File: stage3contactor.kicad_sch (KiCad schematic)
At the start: 3 parts, among them J20 Screw_Terminal_01x06, J21 Screw_Terminal_01x06, J22 Screw_Terminal_01x06

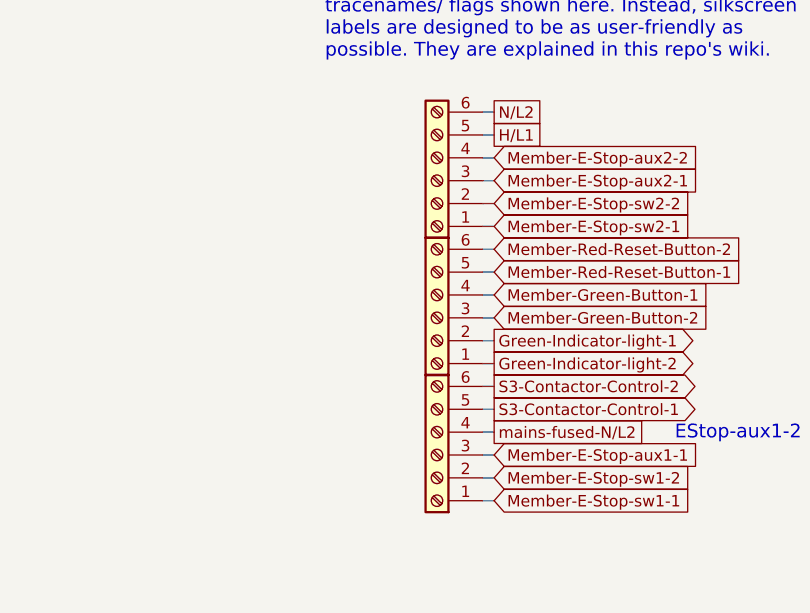
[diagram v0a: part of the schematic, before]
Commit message: 5v binary current and cleanup
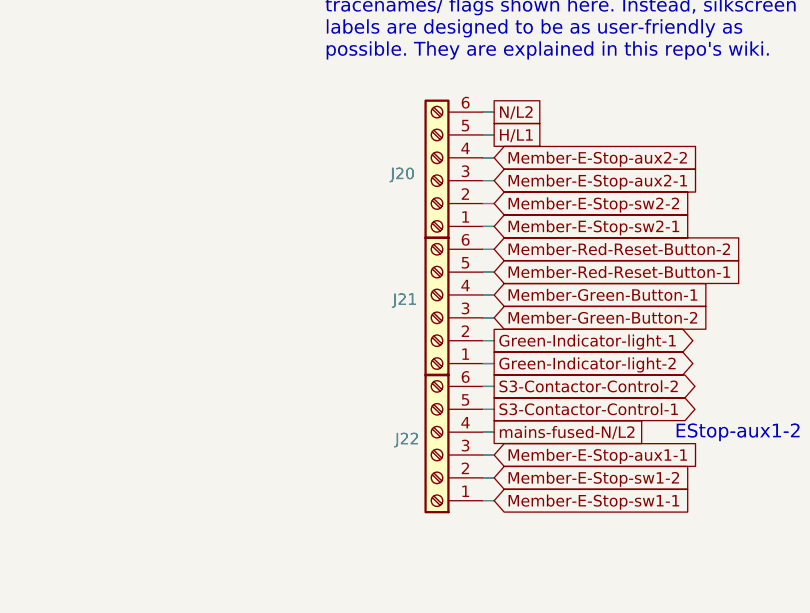
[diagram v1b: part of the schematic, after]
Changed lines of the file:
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@@
 		(on_board yes)
 		(dnp no)
-		(fields_autoplaced yes)
 		(property "Reference" "J20"
-			(at 184.15 78.74 0)
+			(at 180.34 91.948 0)
 			(effects
 				(font
 					(size 1.27 1.27)
 				)
-				(hide yes)
 			)
 		)
@@
 		(on_board yes)
 		(dnp no)
-		(fields_autoplaced yes)
 		(property "Reference" "J21"
-			(at 184.15 93.98 0)
+			(at 180.594 105.918 0)
 			(effects
 				(font
 					(size 1.27 1.27)
 				)
-				(hide yes)
 			)
 		)
@@
 		(on_board yes)
 		(dnp no)
-		(fields_autoplaced yes)
 		(property "Reference" "J22"
-			(at 184.15 109.22 0)
+			(at 180.848 121.412 0)
 			(effects
 				(font
 					(size 1.27 1.27)
 				)
-				(hide yes)
 			)
 		)
